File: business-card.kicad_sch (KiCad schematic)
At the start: 0 parts

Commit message: Add some page metadata
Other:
- title: (none) -> Business Card
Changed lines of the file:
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@@
 	(generator "eeschema")
 	(generator_version "10.0")
-	(paper "A4")
+	(paper "A")
+	(title_block
+		(title "Business Card")
+		(date "2026-10-05")
+		(rev "1")
+	)
 	(sheet_instances
 		(path "/"

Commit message: Placed the CH logo in schematic and pcb
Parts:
- added LOGO1: CH_Logo, business-card:CH_Logo_20mm_SilkScreen, symbol business-card:CH_Logo
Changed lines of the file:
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@@
 		(rev "1")
+	)
+	(symbol
+		(lib_id "business-card:CH_Logo")
+		(at 254 162.56 0)
+		(unit 1)
+		(body_style 1)
+		(exclude_from_sim yes)
+		(in_bom no)
+		(on_board yes)
+		(in_pos_files no)
+		(dnp no)
+		(fields_autoplaced yes)
+		(property "Reference" "LOGO1"
+			(at 260.35 162.5599 0)
+			(show_name no)
+			(do_not_autoplace no)
+			(effects
+				(font
+					(size 1.27 1.27)
+				)
+				(justify left)
+			)
+		)
+		(property "Value" "CH_Logo"
+			(at 254 168.06 0)
+			(hide yes)
+			(show_name no)
+			(do_not_autoplace no)
+			(effects
+				(font
+					(size 1.27 1.27)
+				)
+			)
+		)
+		(property "Footprint" "business-card:CH_Logo_20mm_SilkScreen"
+			(at 254 162.56 0)
+			(hide yes)
+			(show_name no)
+			(do_not_autoplace no)
+			(effects
+				(font
+					(size 1.27 1.27)
+				)
+			)
+		)
+		(property "Datasheet" ""
+			(at 254 162.56 0)
+			(hide yes)
+			(show_name no)
+			(do_not_autoplace no)
+			(effects
+				(font
+					(size 1.27 1.27)
+				)
+			)
+		)
+		(property "Description" "CH monogram with a 20 mm wide front-silkscreen footprint; no electrical pins"
+			(at 254 162.56 0)
+			(hide yes)
+			(show_name no)
+			(do_not_autoplace no)
+			(effects
+				(font
+					(size 1.27 1.27)
+				)
+			)
+		)
+		(instances
+			(project "business-card"
+				(path "/d47d11a5-7f30-4f5f-a335-6efc49b156b4"
+					(reference "LOGO1")
+					(unit 1)
+				)
+			)
+		)
 	)
 	(sheet_instances

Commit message: Add credit card board outline and getting started components
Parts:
- added BT1: 3V, Battery:BatteryHolder_Keystone_1058_1x2032, symbol Device:Battery_Cell
- added D1: red, LED_THT:LED_D5.0mm, symbol Device:LED
- added R1: 1k, Resistor_THT:R_Axial_DIN0309_L9.0mm_D3.2mm_P12.70mm_Horizontal, symbol Device:R_US
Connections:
- new net GND: BT1.2 (-), D1.1 (K)
- new net VCC: BT1.1 (+), R1.1
- new net led: D1.2 (A), R1.2

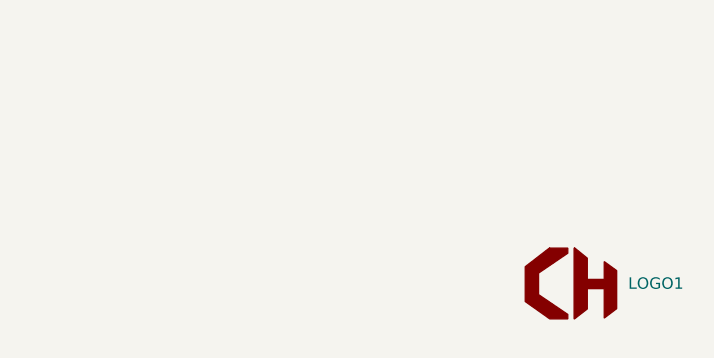
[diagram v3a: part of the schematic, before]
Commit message: Place the contactless tap icon
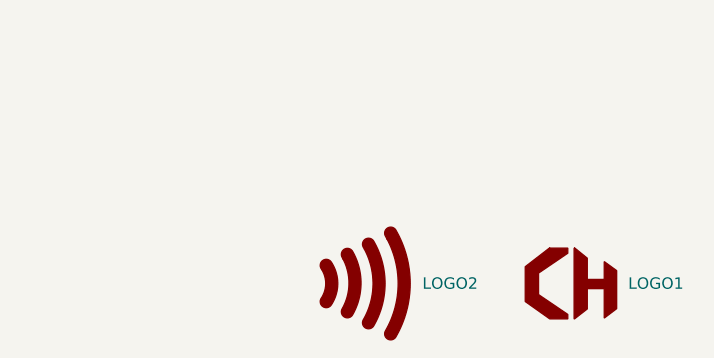
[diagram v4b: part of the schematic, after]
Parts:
- added LOGO2: Contactless_Logo, business-card:Contactless_Logo_10mm_SilkScreen, symbol business-card:Contactless_Logo
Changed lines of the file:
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@@
+	)
+	(symbol
+		(lib_id "business-card:Contactless_Logo")
+		(at 231.14 162.56 0)
+		(unit 1)
+		(body_style 1)
+		(exclude_from_sim yes)
+		(in_bom no)
+		(on_board yes)
+		(in_pos_files no)
+		(dnp no)
+		(fields_autoplaced yes)
+		(property "Reference" "LOGO2"
+			(at 237.49 162.5599 0)
+			(show_name no)
+			(do_not_autoplace no)
+			(effects
+				(font
+					(size 1.27 1.27)
+				)
+				(justify left)
+			)
+		)
+		(property "Value" "Contactless_Logo"
+			(at 231.14 170.3242 0)
+			(hide yes)
+			(show_name no)
+			(do_not_autoplace no)
+			(effects
+				(font
+					(size 1.27 1.27)
+				)
+			)
+		)
+		(property "Footprint" "business-card:Contactless_Logo_10mm_SilkScreen"
+			(at 231.14 162.56 0)
+			(hide yes)
+			(show_name no)
+			(do_not_autoplace no)
+			(effects
+				(font
+					(size 1.27 1.27)
+				)
+			)
+		)
+		(property "Datasheet" "https://www.emvco.com/emv-technologies/emv-contactless-chip/"
+			(at 231.14 162.56 0)
+			(hide yes)
+			(show_name no)
+			(do_not_autoplace no)
+			(effects
+				(font
+					(size 1.27 1.27)
+				)
+			)
+		)
+		(property "Description" "Contactless tap-here indicator with four rounded waves and a 10 mm wide front-silkscreen footprint; no electrical pins"
+			(at 231.14 162.56 0)
+			(hide yes)
+			(show_name no)
+			(do_not_autoplace no)
+			(effects
+				(font
+					(size 1.27 1.27)
+				)
+			)
+		)
+		(instances
+			(project "business-card"
+				(path "/d47d11a5-7f30-4f5f-a335-6efc49b156b4"
+					(reference "LOGO2")
+					(unit 1)
+				)
+			)
+		)
 	)
 	(symbol

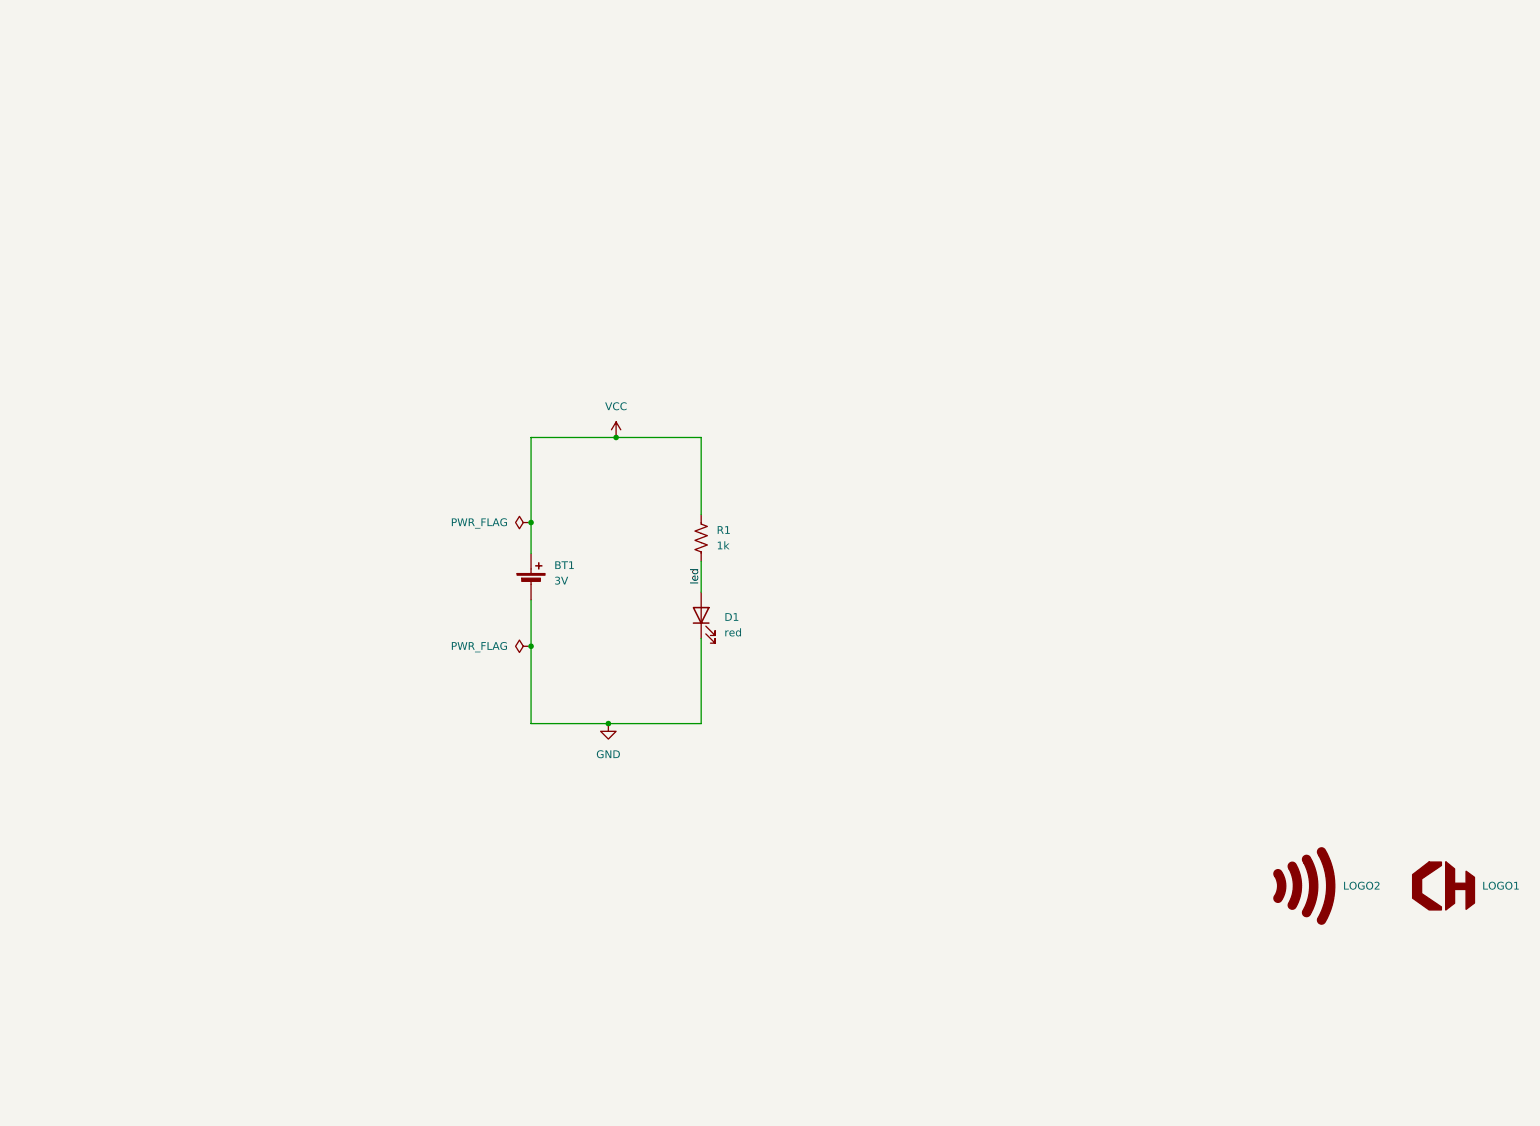
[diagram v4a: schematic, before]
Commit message: First workable version and extra art
* Most components are in the right place and the PCB is routed
* Tag-connect is still enabled and placed/routed
* Board/schematic is customized for CH, but contact info is example data
* Lots of extra symbols and footprints containing alternative art
* Many alternative components
* A few PCB DRC errors remain to be resolved
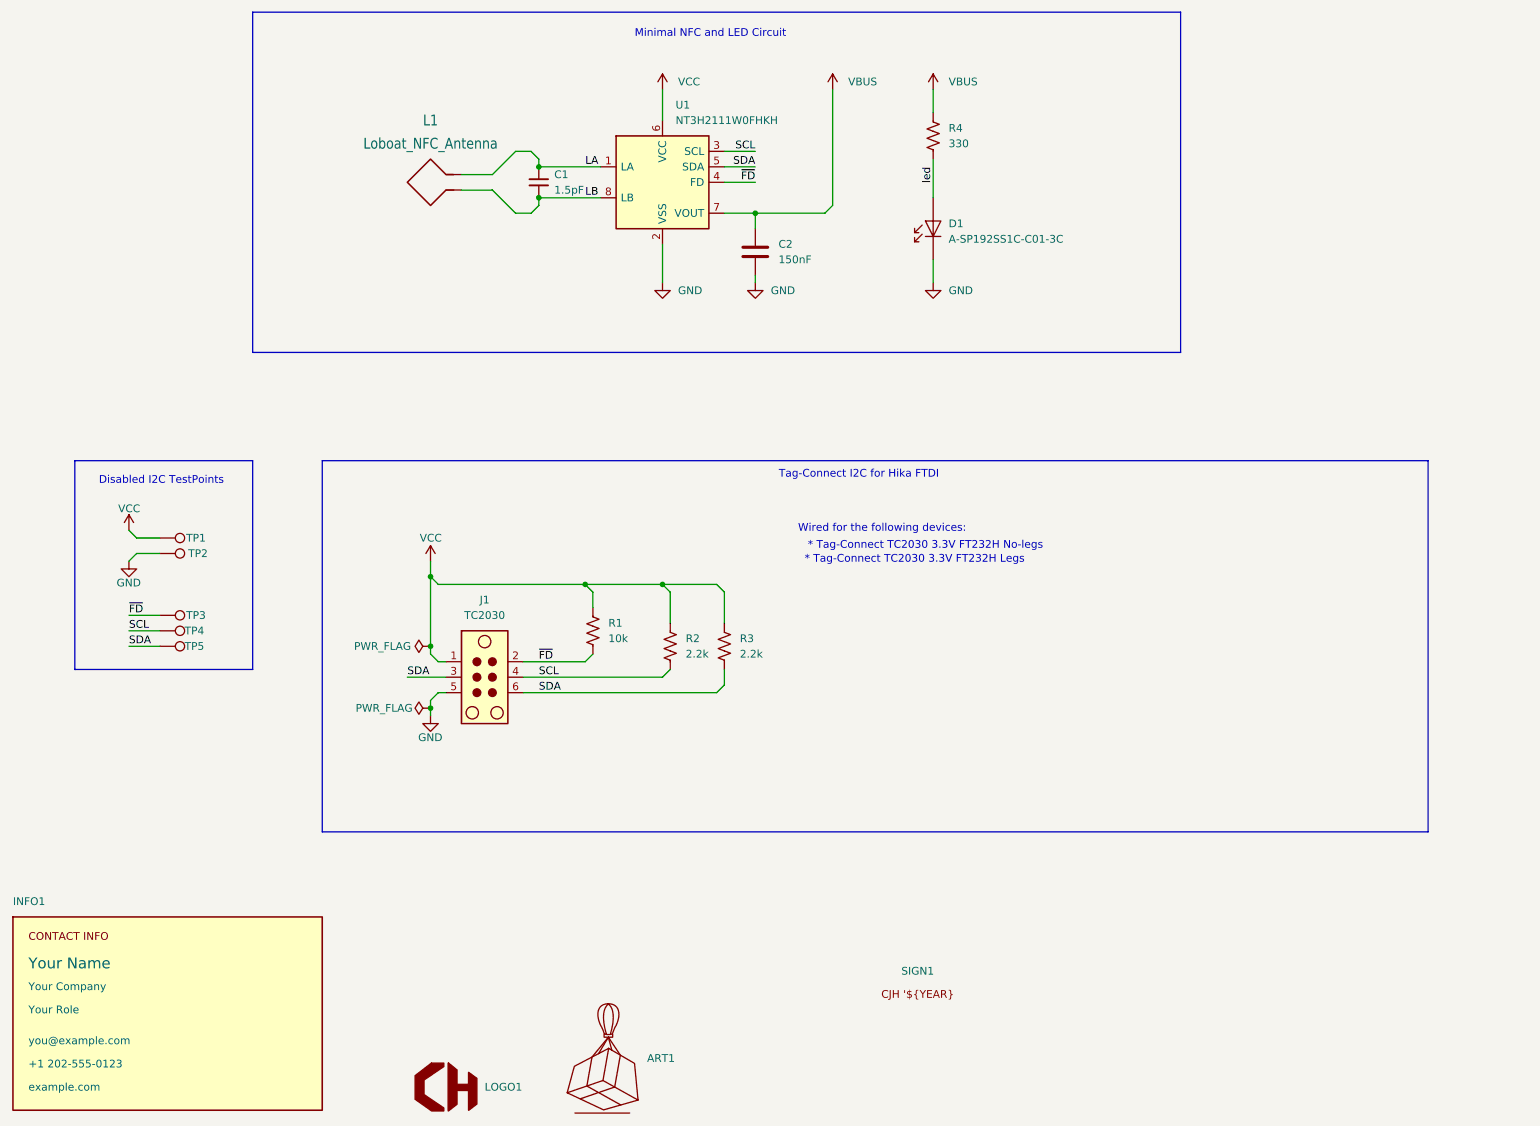
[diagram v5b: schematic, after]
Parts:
- removed BT1: 3V, Battery:BatteryHolder_Keystone_1058_1x2032, symbol Device:Battery_Cell
- removed D1: red, LED_THT:LED_D5.0mm, symbol Device:LED
- removed LOGO2: Contactless_Logo, business-card:Contactless_Logo_10mm_SilkScreen, symbol business-card:Contactless_Logo
- added ART1: LanternLift_GiftWrap, business-card:LanternLift_GiftWrap_Copper_SilkScreen, symbol business-card:LanternLift_GiftWrap
- added C1: 1.5pF, Capacitor_SMD:C_0402_1005Metric_Pad0.74x0.62mm_HandSolder, symbol Device:C_Small
- added C2: 150nF, Capacitor_SMD:C_0402_1005Metric_Pad0.74x0.62mm_HandSolder, symbol Device:C
- added D1: A-SP192SS1C-C01-3C, business-card:Amicc_A-SP192SS1C-C01-3C_SideView, symbol business-card:A-SP192SS1C-C01-3C
- added INFO1: Contact_Info, business-card:Contact_Info_SilkScreen, symbol business-card:Contact_Info
- added J1: TC2030, Connector:Tag-Connect_TC2030-IDC-NL_2x03_P1.27mm_Vertical, symbol Connector:TC2030
- added L1: Loboat_NFC_Antenna, business-card:Loboat_NFC_Antenna_48x25mm_5Turns, symbol business-card:Loboat_NFC_Antenna
- added R1: 10k, Resistor_SMD:R_0402_1005Metric_Pad0.72x0.64mm_HandSolder, symbol Device:R_US
- added R2, R3: 2.2k, Resistor_SMD:R_0402_1005Metric_Pad0.72x0.64mm_HandSolder, symbol Device:R_US
- added SIGN1: CJH_Signature, business-card:CJH_Signature_Copper_Masked, symbol business-card:CJH_Signature
- added TP1, TP2, TP3, TP4, TP5: TestPoint, TestPoint:TestPoint_Pad_D1.0mm, symbol Connector:TestPoint
- added U1: NT3H2111W0FHKH, business-card:NXP_SOT902-3_XQFN-8_1.6x1.6mm, symbol business-card:NT3H2111W0FHKH
- R4: renamed from R1; value 1k -> 330; footprint Resistor_THT:R_Axial_DIN0309_L9.0mm_D3.2mm_P12.70mm_Horizontal -> Resistor_SMD:R_0402_1005Metric_Pad0.72x0.64mm_HandSolder
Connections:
- net GND: now also C2.2, D1.2 (K), J1.5, TP2.1, U1.2 (VSS)
- net VCC: now also J1.1, R1.1, R2.1, R3.1, TP1.1, U1.6 (VCC); no longer R4.1
- net led: now also D1.1 (A)
- new net LA: C1.1, L1.P$2, U1.1 (LA)
- new net LB: C1.2, L1.P$1, U1.8 (LB)
- new net SCL: J1.4, R2.2, TP4.1, U1.3 (SCL)
- new net SDA: J1.3, J1.6, R3.2, TP5.1, U1.5 (SDA)
- new net VBUS: C2.1, R4.1, U1.7 (VOUT)
- new net ~{FD}: J1.2, R1.2, TP3.1, U1.4 (FD)
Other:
- note added: "* Tag-Connect TC2030 3.3V FT232H Legs"
- note added: "* Tag-Connect TC2030 3.3V FT232H No-legs"
- note added: "Disabled I2C TestPoints"
- note added: "Minimal NFC and LED Circuit"
- note added: "Tag-Connect I2C for Hika FTDI"
- note added: "Wired for the following devices:"
- moved on the sheet: LOGO1, R4

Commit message: Change cjh signature and CH logo default footprint
This change snagged some other library changes, too, but functionally
it only makes those two changes.
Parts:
- LOGO1: footprint business-card:CH_Logo_20mm_SilkScreen -> business-card:CH_Logo_20mm_Copper
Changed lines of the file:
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@@
 			)
 		)
-		(property "Footprint" "business-card:CH_Logo_20mm_SilkScreen"
+		(property "Footprint" "business-card:CH_Logo_20mm_Copper"
 			(at 90.17 195.58 0)
 			(hide yes)
